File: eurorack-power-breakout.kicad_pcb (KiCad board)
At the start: 2 copper layers, 22.9 x 53.3 mm, 23 parts, among them J1 upper, J2 lower, J3 bus, J4 PWR, SW1 SW_SPDT

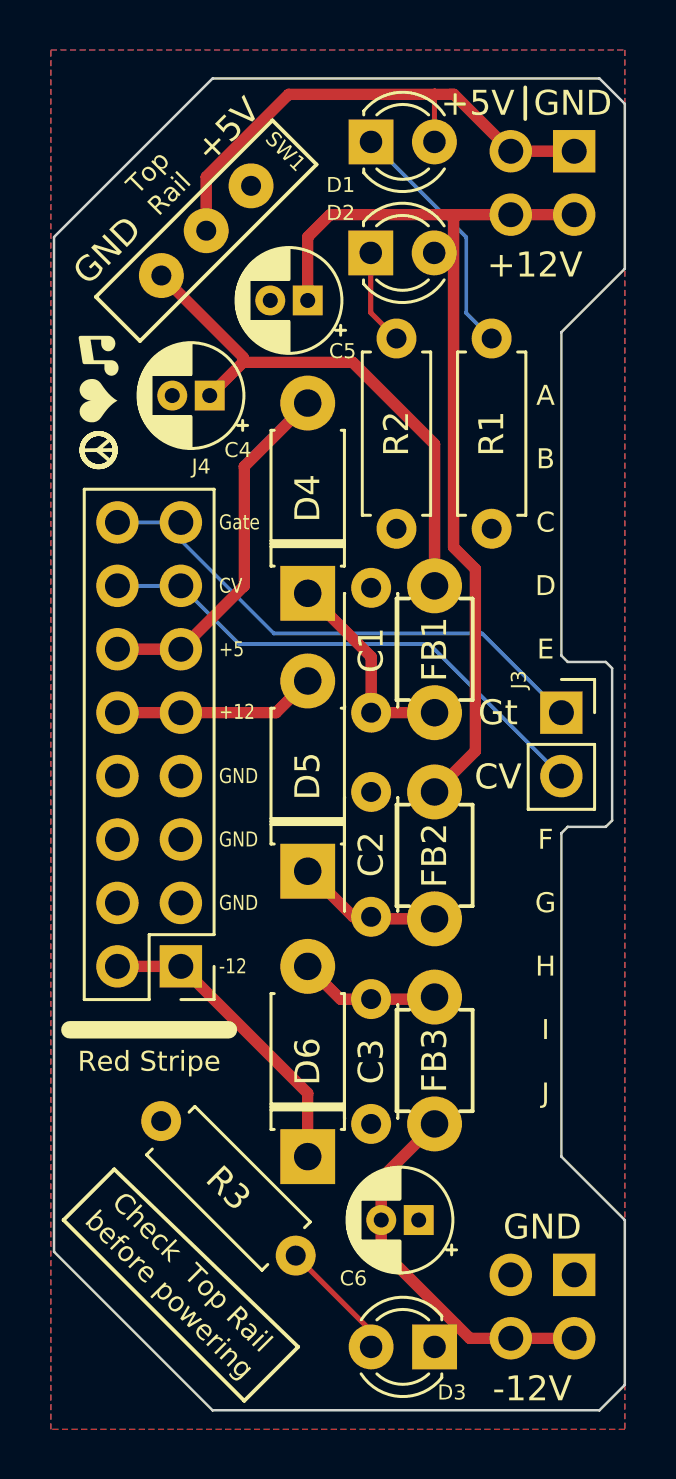
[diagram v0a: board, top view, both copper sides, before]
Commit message: :art: Make some more space around the power connector
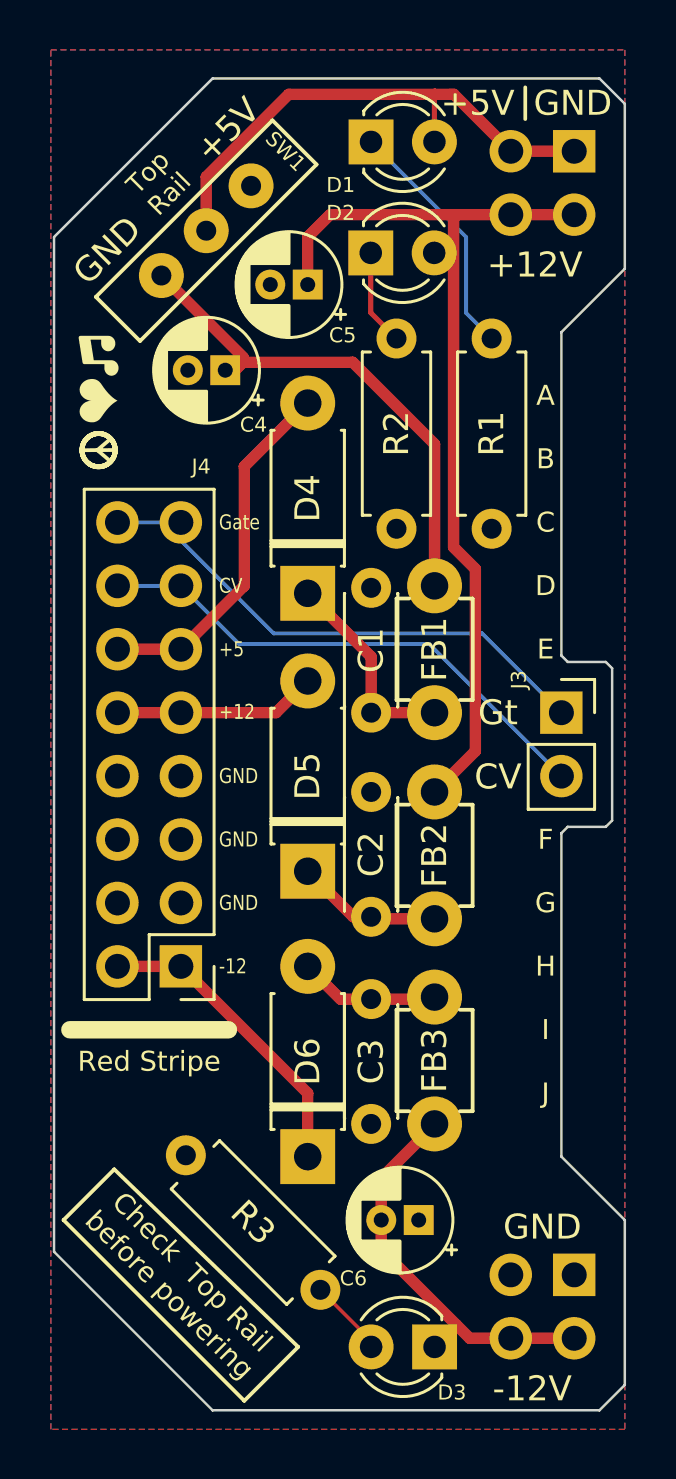
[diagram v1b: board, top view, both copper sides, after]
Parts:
- moved R3 1.69 mm to (137.7, 132.3)
- moved C4 1.19 mm to (133.9, 95.5)
- moved C5 0.63 mm to (137.2, 92.1)
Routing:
- net Net-(R3-Pad1): track 4.90 -> 3.78 mm
- net +5V: track 21.4 -> 20.4 mm
- net +12V: track 37.8 -> 37.2 mm
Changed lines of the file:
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@@
   )
   (footprint "Capacitor_THT:CP_Radial_D4.0mm_P1.50mm" (layer "F.Cu")
-    (at 137.16 92.71 180)
+    (at 137.16 92.075 180)
     (descr "CP, Radial series, Radial, pin pitch=1.50mm, , diameter=4mm, Electrolytic Capacitor")
     (tags "CP Radial series Radial pin pitch 1.50mm  diameter 4mm Electrolytic Capacitor")
@@
   )
   (footprint "Resistor_THT:R_Axial_DIN0207_L6.3mm_D2.5mm_P7.62mm_Horizontal" (layer "F.Cu")
-    (at 136.679077 130.964077 135)
+    (at 137.668 132.334 135)
     (descr "Resistor, Axial_DIN0207 series, Axial, Horizontal, pin pitch=7.62mm, 0.25W = 1/4W, length*diameter=6.3*2.5mm^2, http://cdn-reichelt.de/documents/datenblatt/B400/1_4W%23YAG.pdf")
     (tags "Resistor Axial_DIN0207 series Axial Horizontal pin pitch 7.62mm 0.25W = 1/4W length 6.3mm diameter 2.5mm")
@@
   )
   (footprint "Capacitor_THT:CP_Radial_D4.0mm_P1.50mm" (layer "F.Cu")
-    (at 133.235 96.52 180)
+    (at 133.858 95.504 180)
     (descr "CP, Radial series, Radial, pin pitch=1.50mm, , diameter=4mm, Electrolytic Capacitor")
     (tags "CP Radial series Radial pin pitch 1.50mm  diameter 4mm Electrolytic Capacitor")
@@
   (segment (start 142.24 98.465177) (end 138.961423 95.1866) (width 0.4572) (layer "F.Cu") (net 5))
   (segment (start 134.5684 94.980502) (end 134.5684 95.1866) (width 0.4572) (layer "F.Cu") (net 5))
-  (segment (start 134.5684 95.1866) (end 133.235 96.52) (width 0.4572) (layer "F.Cu") (net 5))
+  (segment (start 133.858 95.504) (end 134.251 95.504) (width 0.4572) (layer "F.Cu") (net 5))
+  (segment (start 134.251 95.504) (end 134.5684 95.1866) (width 0.4572) (layer "F.Cu") (net 5))
   (segment (start 138.961423 95.1866) (end 134.5684 95.1866) (width 0.4572) (layer "F.Cu") (net 5))
-  (segment (start 137.16 90.17) (end 137.16 92.71) (width 0.4572) (layer "F.Cu") (net 6))
   (segment (start 142.24 112.395) (end 143.8734 110.7616) (width 0.4572) (layer "F.Cu") (net 6))
   (segment (start 145.293 89.275) (end 143.135 89.275) (width 0.4572) (layer "F.Cu") (net 6))
@@
   (segment (start 138.055 89.275) (end 137.16 90.17) (width 0.4572) (layer "F.Cu") (net 6))
   (segment (start 147.833 89.275) (end 145.293 89.275) (width 0.4572) (layer "F.Cu") (net 6))
+  (segment (start 137.16 90.17) (end 137.16 92.075) (width 0.4572) (layer "F.Cu") (net 6))
   (segment (start 143.002 102.592023) (end 143.002 89.408) (width 0.4572) (layer "F.Cu") (net 6))
   (segment (start 143.8734 103.463423) (end 143.002 102.592023) (width 0.4572) (layer "F.Cu") (net 6))
@@
   (segment (start 134.409 106.469) (end 142.029 106.469) (width 0.1524) (layer "B.Cu") (net 15))
   (segment (start 129.54 104.14) (end 132.08 104.14) (width 0.1524) (layer "B.Cu") (net 15))
+  (segment (start 139.7 134.366) (end 139.7 134.62) (width 0.1524) (layer "F.Cu") (net 16))
   (segment (start 139.685 133.97) (end 139.685 134.62) (width 0.2032) (layer "F.Cu") (net 16))
-  (segment (start 136.679077 130.964077) (end 139.685 133.97) (width 0.2032) (layer "F.Cu") (net 16))
+  (segment (start 137.668 132.334) (end 139.7 134.366) (width 0.1524) (layer "F.Cu") (net 16))
   (zone (net 2) (net_name "GND") (layer "F.Cu") (hatch edge 0.508)
     (connect_pads (clearance 0.3048))

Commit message: :art: Make room for a box pwr connector
The courtyard drawing is not 100% exact, but sufficient for this
application.
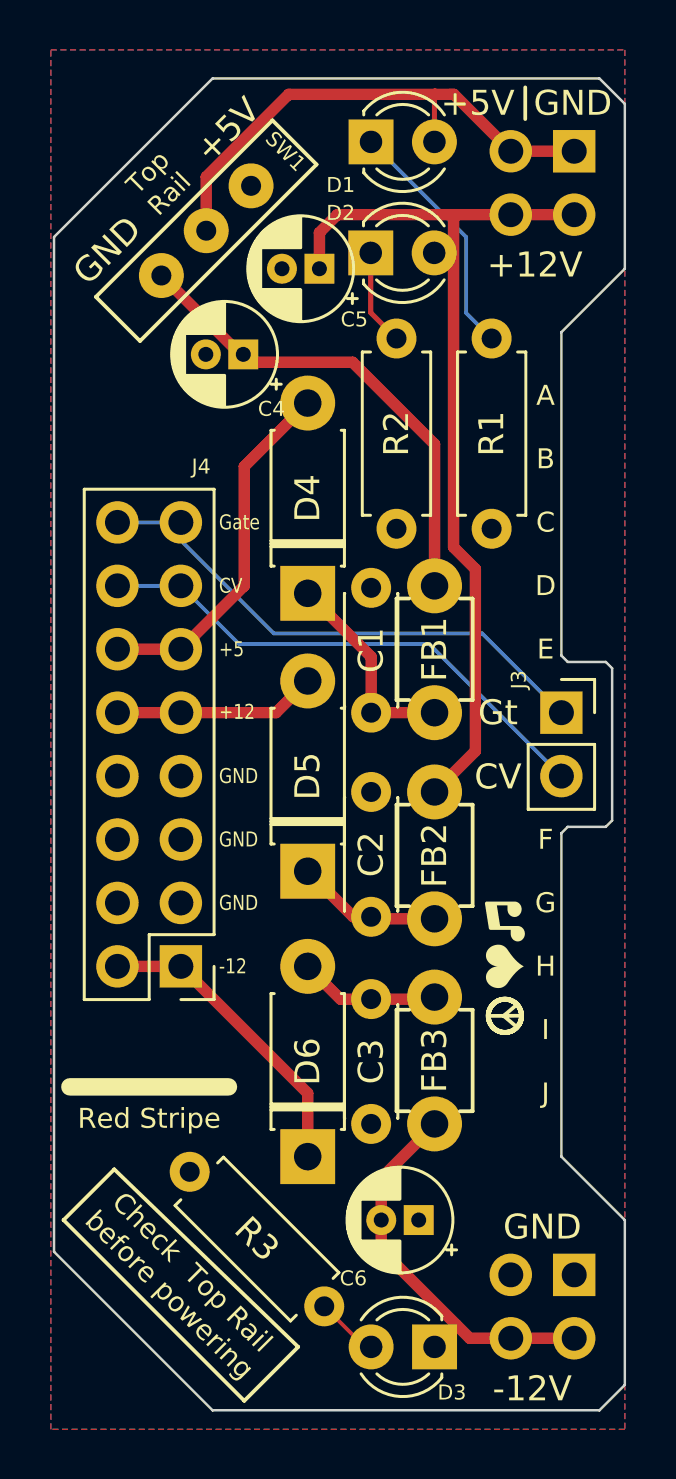
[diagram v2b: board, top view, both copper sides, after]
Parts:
- moved C4 0.96 mm to (134.6, 94.9)
- moved C5 0.79 mm to (137.6, 91.4)
- moved R3 0.68 mm to (137.8, 133.0)
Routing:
- net +12V: track 37.2 -> 36.2 mm
- net +5V: track 20.4 -> 19.5 mm

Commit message: :arrow_up: Upgrade to Kicad 7
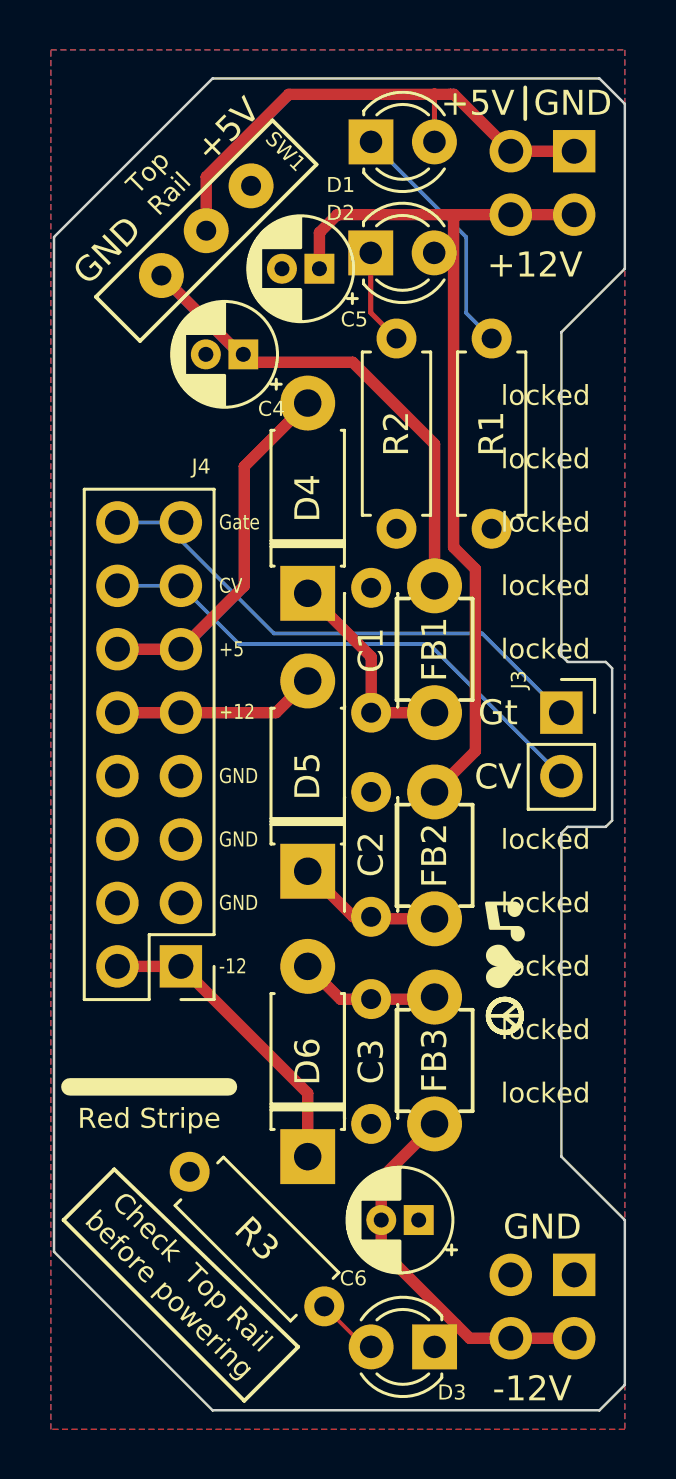
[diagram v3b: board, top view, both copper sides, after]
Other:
- board text added: "locked"
- board text removed: "A"
- board text removed: "B"
- board text removed: "C"
- board text removed: "D"
- board text removed: "E"
- board text removed: "F"
- board text removed: "G"
- board text removed: "H"
- board text removed: "I"
- board text removed: "J"

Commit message: :ok_hand: Fix DRC findings
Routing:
- net Net-(D3-A): track 3.45 -> 2.30 mm
- net +5V: track 19.5 -> 20.4 mm
- net -12V: track 16.4 -> 15.8 mm
